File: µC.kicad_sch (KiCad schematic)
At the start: 17 parts, among them J4 USB_C_Receptacle_USB2.0_14P, SW4 SW_Push, SW6 SW_Push, U2 ESP32-S3-WROOM-1

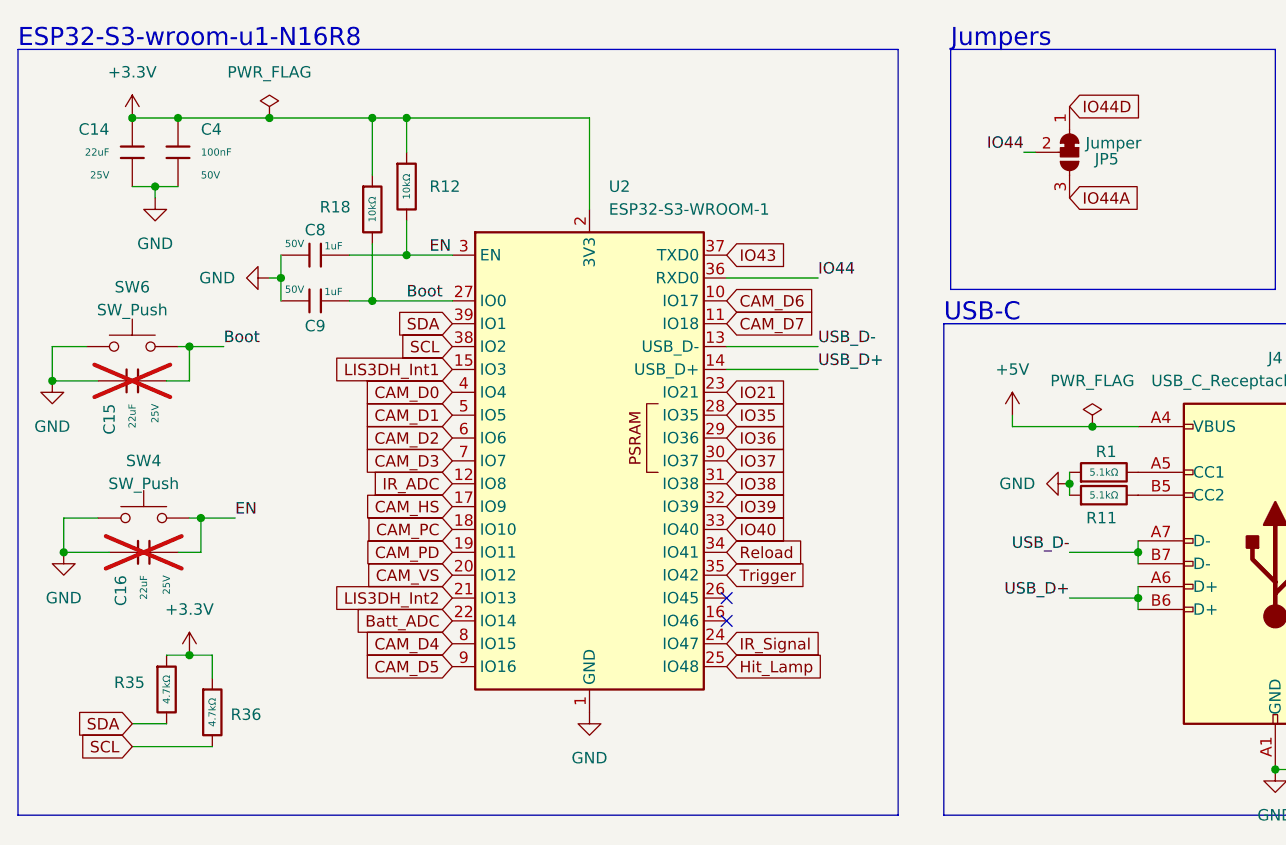
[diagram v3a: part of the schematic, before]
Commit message: replaced ir-led constant current circuit
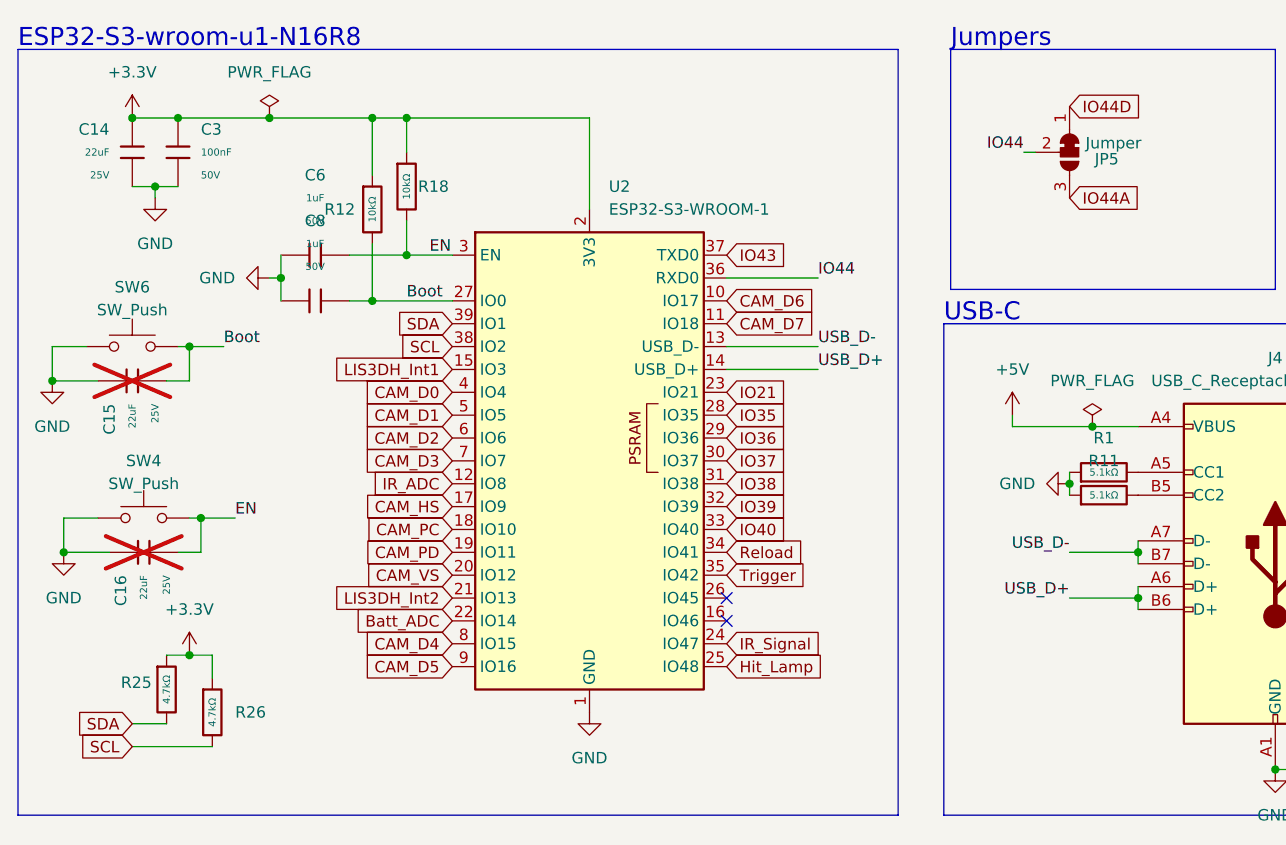
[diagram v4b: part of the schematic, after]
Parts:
- removed C4: 100nF, PCM_JLCPCB:C_0603, symbol PCM_JLCPCB-Capacitors:0603,100nF
- removed C8, C9: 1uF, PCM_JLCPCB:C_0603, symbol PCM_JLCPCB-Capacitors:0603,1uF
- removed R1, R11: 5.1kΩ, PCM_JLCPCB:R_0603, symbol PCM_JLCPCB-Resistors:0603,5.1kΩ
- removed R12, R18: 10kΩ, PCM_JLCPCB:R_0603, symbol PCM_JLCPCB-Resistors:0603,10kΩ
- removed R35, R36: 4.7kΩ, PCM_JLCPCB:R_0603, symbol PCM_JLCPCB-Resistors:0603,4.7kΩ
- added C3: 100nF, PCM_JLCPCB:C_0805, symbol PCM_JLCPCB-Capacitors:0805,100nF,(2)
- added C6, C8: 1uF, PCM_JLCPCB:C_0805, symbol PCM_JLCPCB-Capacitors:0805,1uF
- added R1, R11: 5.1kΩ, PCM_JLCPCB:R_0805, symbol PCM_JLCPCB-Resistors:0805,5.1kΩ
- added R12, R18: 10kΩ, PCM_JLCPCB:R_0805, symbol PCM_JLCPCB-Resistors:0805,10kΩ
- added R25, R26: 4.7kΩ, PCM_JLCPCB:R_0805, symbol PCM_JLCPCB-Resistors:0805,4.7kΩ
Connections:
- net +3.3V: now also C3.1, R12.1, R18.1, R25.1, R26.1
- net Boot: now also C8.2, R12.2
- net EN: now also C6.2, R18.2
- net GND: now also C3.2, C6.1, C8.1, R1.1, R11.1
- net SCL: now also R26.2
- net SDA: now also R25.2
- net at J4.B5 (CC2): now also R11.2
- net at J4.A5 (CC1): now also R1.2

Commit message: pcb layout designing
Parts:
- J4: footprint (none) -> Connector_USB:USB_C_Receptacle_GCT_USB4085
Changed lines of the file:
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@@
 			)
 		)
-		(property "Footprint" ""
+		(property "Footprint" "Connector_USB:USB_C_Receptacle_GCT_USB4085"
 			(at 152.4 74.93 0)
 			(effects

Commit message: pcb didn't commit correctly
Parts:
- removed JP5: Jumper, Jumper:SolderJumper-3_P1.3mm_Bridged12_RoundedPad1.0x1.5mm_NumberLabels, symbol Jumper:SolderJumper_3_Bridged12
- added PN1: ~, PCM_JLCPCB:Part_Num_JLCPCB, symbol PCM_JLCPCB-Manufacturing:Part Number, PCM_JLCPCB, 0.8x0.15mm
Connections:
- net CAM_D1 is gone; now on net Hit_Lamp: U2.5 (IO5)
- net CAM_D2 is gone; now on net IR_Signal: U2.6 (IO6)
- net CAM_VS is gone; now on net LIS3DH_Int1: U2.20 (IO12)
- net Hit_Lamp: no longer U2.25 (IO48)
- net IR_Signal: no longer U2.24 (IO47)
- net LIS3DH_Int1: no longer U2.15 (IO3)
- net CAM_D0: no longer names the net of U2.4 (IO4)
- net CAM_D3: no longer names the net of U2.7 (IO7)
- net CAM_D4: no longer names the net of U2.8 (IO15)
- net CAM_D5: no longer names the net of U2.9 (IO16)
- net CAM_D6: no longer names the net of U2.10 (IO17)
- net CAM_D7: no longer names the net of U2.11 (IO18)
- net CAM_HS: no longer names the net of U2.17 (IO9)
- net CAM_PC: no longer names the net of U2.18 (IO10)
- net CAM_PD renamed IO11
- no-connect marks 2 -> 14
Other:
- note removed: "Jumpers"
